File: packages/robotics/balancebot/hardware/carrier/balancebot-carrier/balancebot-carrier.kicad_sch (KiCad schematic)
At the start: 19 parts, among them J1 JST-XH pack in, J2 LM2596 module, J3 GY-521 MPU6050, J4 Motor left, J5 Motor right, U1 XIAO RP2350

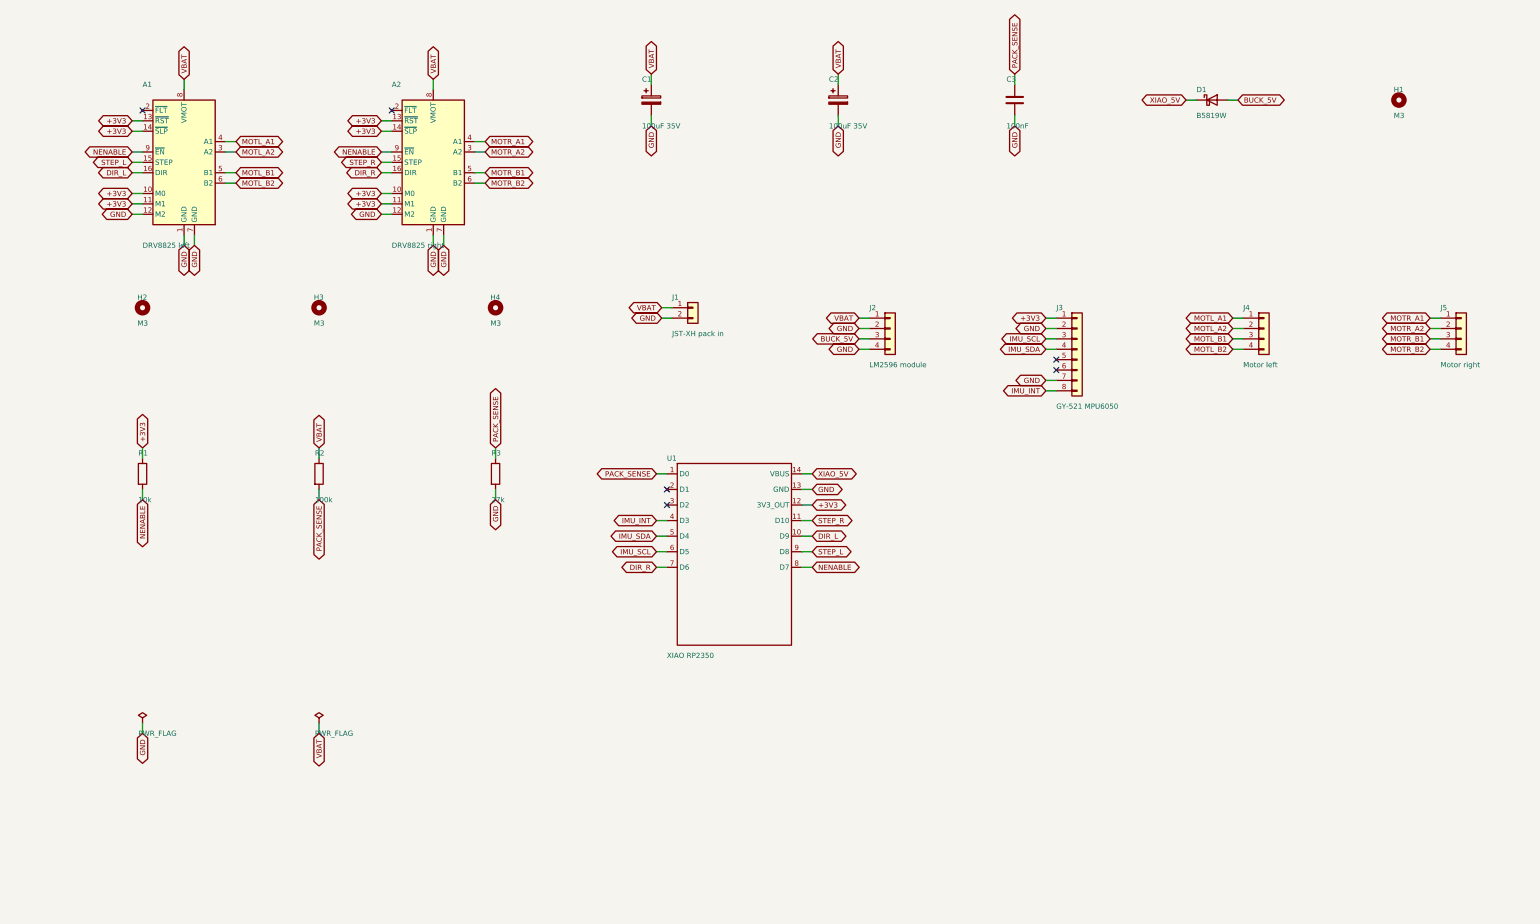
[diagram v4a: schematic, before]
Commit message: fix(balancebot): pre-order carrier fixes, reverse-polarity input, stitching vias (#822)
* feat(kicad): [fanout] own pads take a via of their own

A pad joined by a fixed track to another pad that has a via counted as
having one, so the integrated carrier's buck GND pin (U10:1), tied under
the package to C11, never got a via beside it. An `own` pad ignores that
chain and takes its own via (TI's first layout rule for the TPS563208).

Co-Authored-By: Claude Opus 5.5 <noreply@anthropic.com>
Claude-Session: https://claude.ai/code/session_01DgeoMcrSCUfJwedu77q6oo

* fix(robocar-unified-integrated): fix the power paths the layout review found

The pre-fab layout review of the integrated carrier found the buck's output
capacitors 75 mm of track from L1 and the pack input on a 0.25 mm track,
neither visible to a gate. Fixed tracks in board.toml now:

- chain C13, C14 and C20 onto L1's output pad, and run the trunk and a 1 mm
  east branch (C7, the LDO, FB1) from that node;
- give the feedback divider its own sense track from C20;
- carry PACK_IN on 2 mm from the XT30 to F1;
- run C12 straight into L1 so U10's GND pin gets its own via.

C5, C6 and C18 move beside the pins they decouple, C21 adds 10 uF at the
TB6612FNG's VM1, the GND pour stops 1 mm short of the mouse-bite slot, and
R26 becomes 36 k so EN is guaranteed on by 6.3 V rather than 7.2 V. The
README records each finding with before and after measurements, and that
the pack takes an external 2S BMS.

Routed with KiCad 10.0.7 (the stamp records it), not the pinned 10.0.6.

Co-Authored-By: Claude Opus 5.5 <noreply@anthropic.com>
Claude-Session: https://claude.ai/code/session_01DgeoMcrSCUfJwedu77q6oo

* docs(robocar-unified-integrated): correct the layout fixes table

The M1 row said VM1 and the servos reach L1 with no via. They still share
one 0.8/0.4 mm via: the measuring script joined B.Cu track ends to F.Cu
tracks they only cross. The m1, m2 and m5 rows take the second review's
layer-aware measurements, and its find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
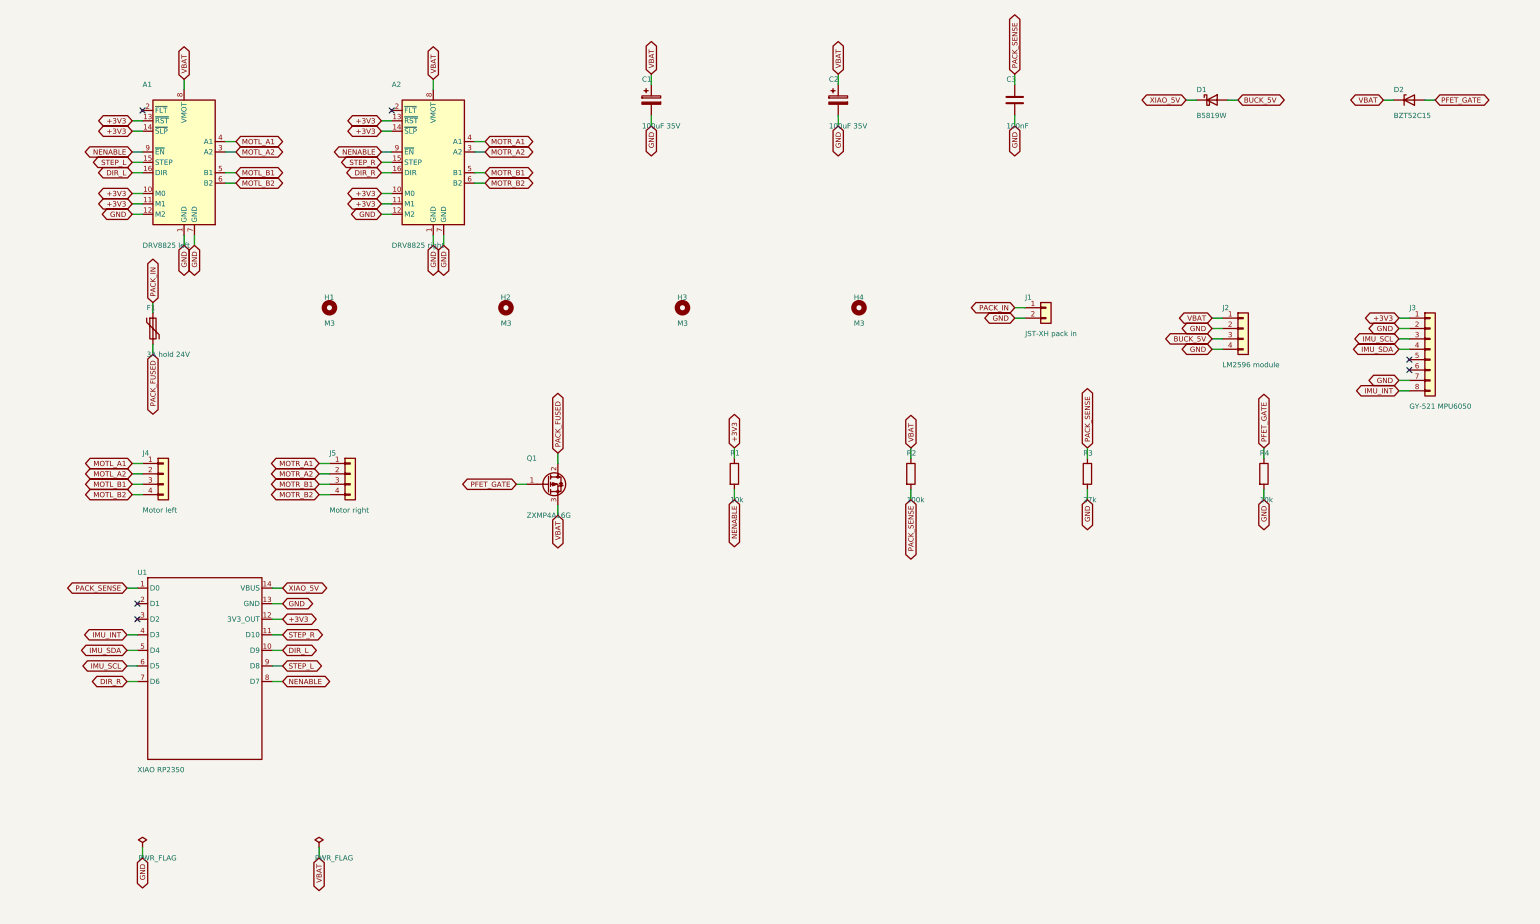
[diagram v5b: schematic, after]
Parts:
- added D2: BZT52C15, Diode_SMD:D_SOD-123, symbol Device:D_Zener
- added F1: 3A hold 24V, Fuse:Fuse_1812_4532Metric_Pad1.30x3.40mm_HandSolder, symbol Device:Polyfuse
- added Q1: ZXMP4A16G, Package_TO_SOT_SMD:SOT-223-3_TabPin2, symbol Transistor_FET:ZXMP4A16G
- added R4: 10k, Resistor_SMD:R_0805_2012Metric_Pad1.20x1.40mm_HandSolder, symbol Device:R
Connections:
- net GND: now also R4.2
- net VBAT: now also D2.1 (K), Q1.3 (S); no longer J1.1 (Pin_1)
- new net PACK_FUSED: F1.2, Q1.2 (D)
- new net PACK_IN: F1.1, J1.1 (Pin_1)
- new net PFET_GATE: D2.2 (A), Q1.1 (G), R4.1
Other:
- moved on the sheet: H1, H2, H3, H4, J1, J2, J3, J4, J5, R1, R2, R3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
